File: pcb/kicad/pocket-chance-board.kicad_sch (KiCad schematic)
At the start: 123 parts, among them J1 SWD, J2 USB4085-GF-A, J3 LiPo JST-PH 2.0mm (pin 1 = + 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, J4 LCD 1.54in ST7789 module, JST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, J5 Speaker JST-PH, J6 microSD Molex 104031-0811, J7 STEMMA QT, J8 Expansion, Q1 FS8205A, Q2 DMG2305UX, SW1 BOOT, SW10 DPAD LEFT PTS645SM43SMTR92, SW11 DPAD RIGHT PTS645SM43SMTR92, SW12 DPAD PRESS PTS645SM43SMTR92, SW2 RESET, SW3 POWER PCM12, SW4 A PTS125SM43SMTR2LFS, SW5 B PTS125SM43SMTR2LFS, SW6 X PTS125SM43SMTR2LFS, SW7 Y PTS125SM43SMTR2LFS, SW8 DPAD UP PTS645SM43SMTR92, SW9 DPAD DOWN PTS645SM43SMTR92, U1 RP2350A, U10 LSM6DSOXTR, U11 RM2, U2 W25Q128JVSIQ, U3 APS6404L-3SQR-SN, U4 USBLC6-2SC6, U5 BQ24074RGTR, U6 TPS63001DRCR, U7 DW01A, U8 PAM8302AADCR, U9 DS3231MZ+, Y1 12MHz ABM8-272-T3

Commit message: AUDIT-2 fixes: guard FET orientation (#1), gated battery divider (#2), 3-pin cell socket with NTC pin (#7/#8), RTC INT pull-up and series R (#9), named L2 and rated caps (#10), second DVDD 4.7uF (#11), amp bypass and SD delay (#12), R15 not fitted (#13), Q2 value (#14)
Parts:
- removed J3: LiPo JST-PH 2.0mm (pin 1 = + RED WIRE), Connector_JST:JST_PH_S2B-PH-SM4-TB_1x02-1MP_P2.00mm_Horizontal, symbol Connector:Conn_01x02_Socket
- added C40: 4.7uF, Capacitor_SMD:C_0402_1005Metric, symbol Device:C
- added C41, C42: 1uF, Capacitor_SMD:C_0603_1608Metric, symbol Device:C
- added J3: LiPo JST-PH 2.0mm (1 = + RED, 2 = -, 3 = NTC), Connector_JST:JST_PH_S3B-PH-SM4-TB_1x03-1MP_P2.00mm_Horizontal, symbol Connector:Conn_01x03_Socket
- added Q3: 2N7002, Package_TO_SOT_SMD:SOT-23, symbol Transistor_FET:2N7002
- added Q4: AO3401A, Package_TO_SOT_SMD:SOT-23, symbol Transistor_FET:AO3401A
- added R39: 100k, Resistor_SMD:R_0402_1005Metric, symbol Device:R
- added R42: 10k, Resistor_SMD:R_0402_1005Metric, symbol Device:R
- added R43: 1k, Resistor_SMD:R_0402_1005Metric, symbol Device:R
- added R44: 47k, Resistor_SMD:R_0402_1005Metric, symbol Device:R
- C23: value 10uF -> 10uF 16V X5R; footprint Capacitor_SMD:C_0603_1608Metric -> Capacitor_SMD:C_0805_2012Metric
- C25, C26: value 10uF -> 10uF 10V X5R; footprint Capacitor_SMD:C_0603_1608Metric -> Capacitor_SMD:C_0805_2012Metric
- J8: value Expansion -> Expansion (6 = VBAT_SENSE ADC node, not free GPIO)
- JP2: value RTC INT to GP14 -> RTC INT to GP14 (open; close only after firmware sets IMU INT1 open-drain, active-low)
- L2: value 2.2uH -> 2.2uH ASPIAIG-F4020-2R2M; footprint Inductor_SMD:L_1210_3225Metric -> Inductor_SMD:L_Abracon_ASPIAIG-F4020
- Q2: value DMG2305UX -> AO3401A
- R15: value 3.0k -> 3.0k DNP; now not fitted
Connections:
- net +3V3: now also C41.1, Q3.1 (G), R42.1, R44.1; no longer U8.1 (~{SD})
- net 1V1: now also C40.1
- net BAT+: now also Q4.2 (S), R39.1; no longer R23.1
- net BAT-: now also J3.2 (Pin_2)
- net CELL_G: now also Q2.2 (S); no longer Q2.3 (D)
- net CELL_P: now also Q2.3 (D), J3.1 (Pin_1); no longer Q2.2 (S)
- net GND: now also C40.2, C41.2, C42.2, Q3.2 (S)
- net RTC_INT: now also R42.2, R43.1; no longer JP2.1 (A)
- net TS: now also J3.3 (Pin_3)
- new net AMP_SD: C42.1, R44.2, U8.1 (~{SD})
- new net DIV_PG: Q3.3 (D), Q4.1 (G), R39.2
- new net DIV_TOP: Q4.3 (D), R23.1
- new net RTC_INT_R: JP2.1 (A), R43.2

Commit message: AUDIT-2 response, battery guidance, owner warning on the schematic; PCB-001, PARTS, STAGE2, DR-033 updated for the fixes
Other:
- note added: "BATTERY (PCB-001, owner decision 2026-10-04): one protected LiPo pouch cell, 1000 mAh or more, rated 0.5 C charge, charge temperature 0 to 45 C, JST-PH plug, + on pin 1 (red wire). Charge current 494 mA (R14 1.8k; 3.6k for 500 mAh). The charger does NOT sense the cell's temperature with a two-wire cell (R12 10k fitted = check bypassed); it relies on the cell's own protection board and the 0.5 C r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"
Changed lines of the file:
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@@
+		)
+	)
+	(text "BATTERY (PCB-001, owner decision 2026-10-04): one protected LiPo pouch cell, 1000 mAh or more, rated 0.5 C charge, charge temperature 0 to 45 C, JST-PH plug, + on pin 1 (red wire). Charge current 494 mA (R14 1.8k; 3.6k for 500 mAh). The charger does NOT sense the cell's temperature with a two-wire cell (R12 10k fitted = check bypassed); it relies on the cell's own protection board and the 0.5 C rate. A cell with a thermistor lead goes on pin 3: then remove R12. First power-ups: current-limited supply, no cell; then cell alone; then both. Charge on a non-flammable surface, never unattended."
+		(exclude_from_sim no)
+		(at 290 470 0)
+		(effects
+			(font
+				(size 1.5 1.5)
+			)
+			(justify left top)
 		)
 	)

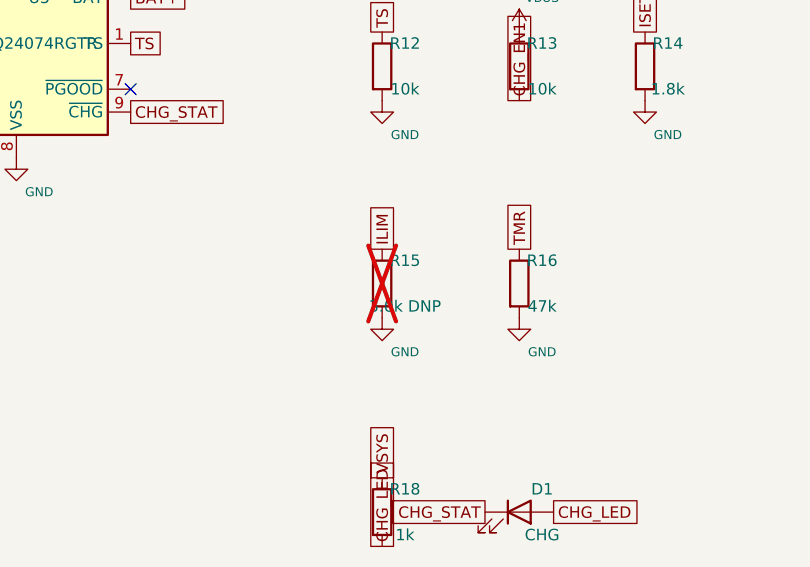
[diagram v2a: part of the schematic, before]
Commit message: AUDIT-3 #2: fit R15 (ILIM), the BQ24074 disables all charging with ILIM open; schematic rev 0.4
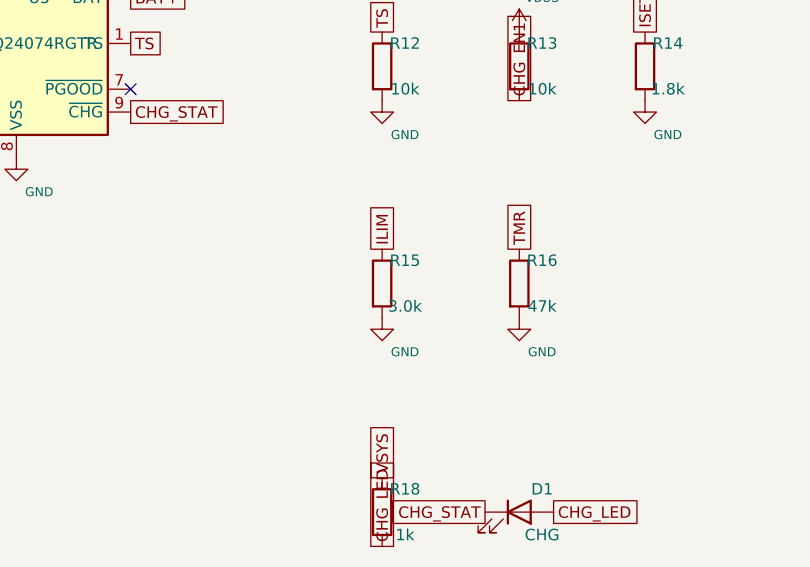
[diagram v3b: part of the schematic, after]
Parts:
- R15: value 3.0k DNP -> 3.0k; now fitted
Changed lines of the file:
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@@
 		(title "Pocket Chance board, spin 1")
 		(date "2026-10-04")
-		(rev "0.3")
+		(rev "0.4")
 		(company "Pocket Chance")
 		(comment 1 "Generated by pcb/tools/gen_sch.py from the connection table. Label-based: every pin carries its net name.")
@@
 		(in_bom yes)
 		(on_board yes)
-		(dnp yes)
+		(dnp no)
 		(property "Reference" "R15"
 			(at 342.9 207.01 0)
@@
 			)
 		)
-		(property "Value" "3.0k DNP"
+		(property "Value" "3.0k"
 			(at 342.9 212.09 0)
 			(effects

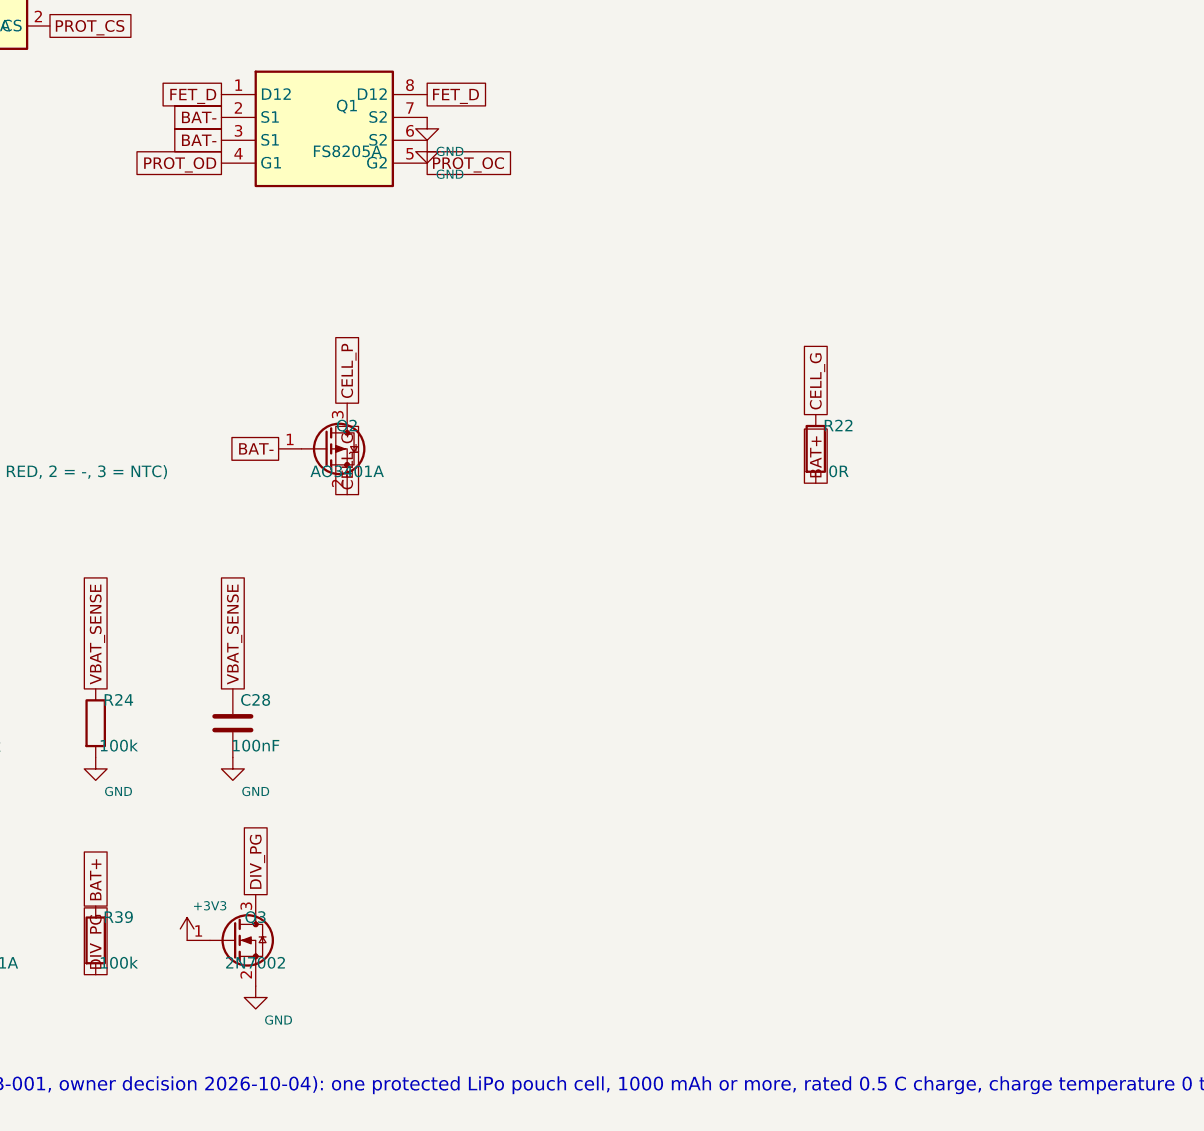
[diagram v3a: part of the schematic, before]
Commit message: Rev 0.5: polarity-sensing reverse guard (AUDIT-3 #1, HR-P05 part 4), RM2 land pattern corrected with courtyard margin and keep-out rule area (AUDIT-3 #3), charge-rate wording (AUDIT-3 #2)
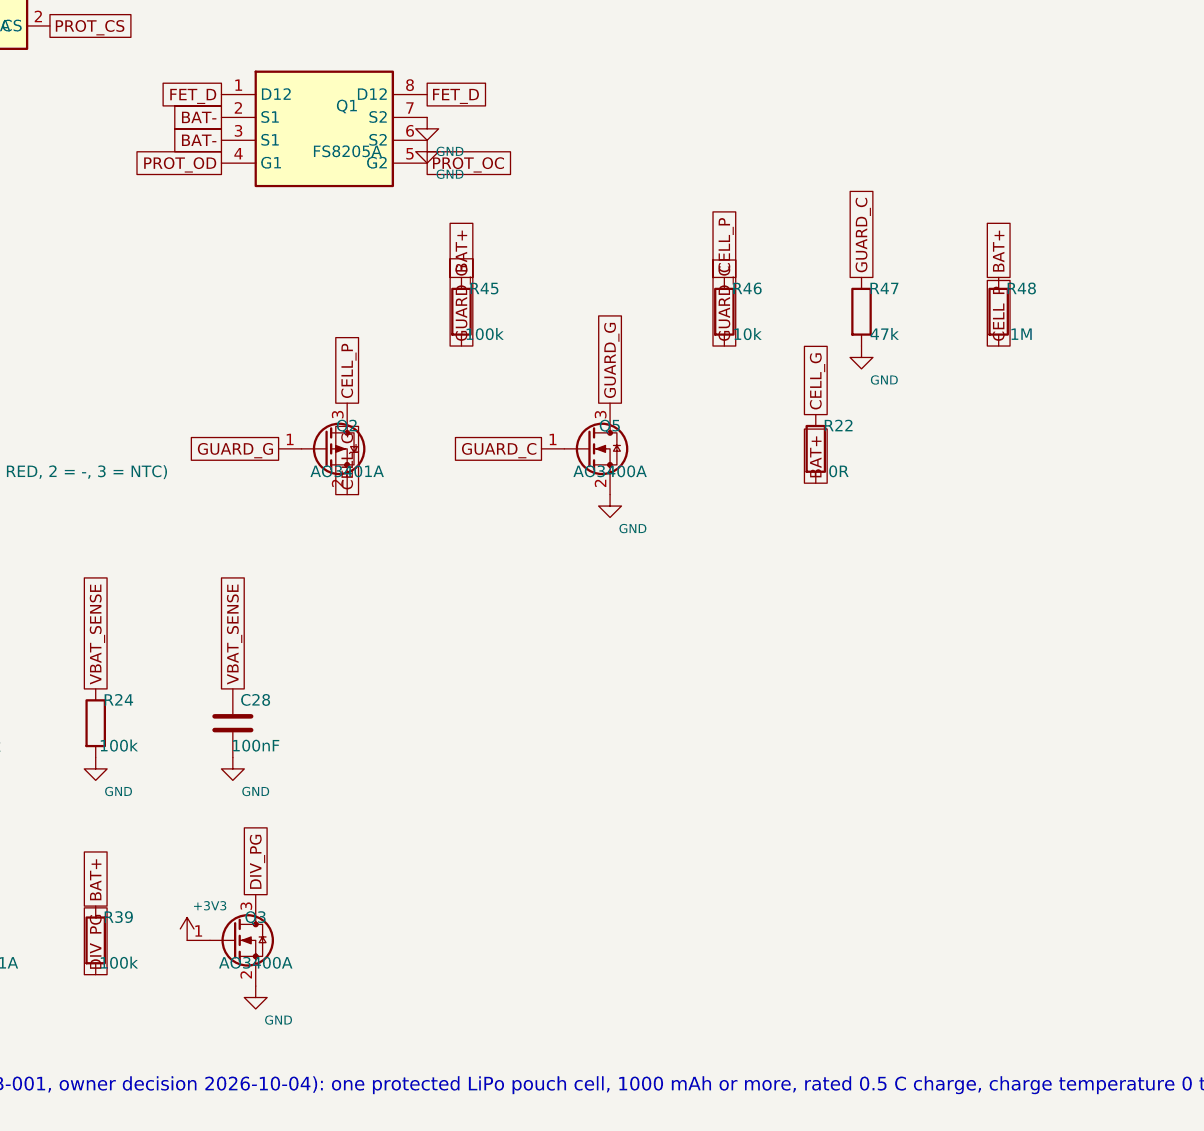
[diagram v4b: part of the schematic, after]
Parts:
- removed Q3: 2N7002, Package_TO_SOT_SMD:SOT-23, symbol Transistor_FET:2N7002
- added Q3, Q5: AO3400A, Package_TO_SOT_SMD:SOT-23, symbol Transistor_FET:AO3400A
- added R45: 100k, Resistor_SMD:R_0402_1005Metric, symbol Device:R
- added R46: 10k, Resistor_SMD:R_0402_1005Metric, symbol Device:R
- added R47: 47k, Resistor_SMD:R_0402_1005Metric, symbol Device:R
- added R48: 1M, Resistor_SMD:R_0402_1005Metric, symbol Device:R
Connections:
- net +3V3: now also Q3.1 (G)
- net BAT+: now also R45.1, R48.1
- net BAT-: no longer Q2.1 (G)
- net CELL_P: now also R46.1, R48.2
- net DIV_PG: now also Q3.3 (D)
- net GND: now also Q3.2 (S), Q5.2 (S), R47.2
- new net GUARD_C: Q5.1 (G), R46.2, R47.1
- new net GUARD_G: Q2.1 (G), Q5.3 (D), R45.2
